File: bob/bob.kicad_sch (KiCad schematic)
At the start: 28 parts, among them J1 PROG, J2 PWR, J3 BB, U1 PAN2110P0AA, U2 LM1117MP-3.3, U3 PY32F030K1xTx, Y1 16MHz

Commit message: WIP
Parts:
- removed C1, C2, C3, C4: NC, Capacitor_SMD:C_0805_2012Metric, symbol Device:C
- removed R2: 0R, Resistor_SMD:R_0805_2012Metric, symbol Device:R
- added JP2: I2C/SPI, Jumper:SolderJumper-3_P2.0mm_Open_TrianglePad1.0x1.5mm, symbol Jumper:SolderJumper_3_Open
- R1: value 0R -> 10k
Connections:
- net +3V3: now also JP2.3 (B)
- net GND: now also JP2.1 (A)
- net PROG_RXD: now also J1.3 (Pin_3); no longer J1.5 (Pin_5)
- net PROG_TXD: now also J1.5 (Pin_5); no longer J1.3 (Pin_3)
- net ~{RF_CS}: now also R1.1
- net at U1.5 (XC1): now also Y1.1
- net at U1.8 (ANT): now also A1.1 (A); no longer R1.1
- net at R1.2: now also JP2.2 (C); no longer A1.1 (A)
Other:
- moved on the sheet: A1, Y1

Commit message: bob 1.3
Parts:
- added R2, R5: 4k7, Resistor_SMD:R_0805_2012Metric, symbol Device:R
- J3: footprint Connector_PinHeader_2.54mm:PinHeader_1x24_P2.54mm_Vertical -> Connector_PinHeader_2.54mm:PinHeader_1x26_P2.54mm_Vertical; symbol Connector:Conn_01x24_Pin -> Connector:Conn_01x26_Pin
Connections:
- net +3V3: now also R2.2, R5.2
- net GND: now also J3.26 (Pin_26); no longer J3.24 (Pin_24)
- net RF_CLK renamed PA9
- net PA9: now also J3.25 (Pin_25), R5.1
- net RF_DIO renamed PA7
- net PA7: now also J3.24 (Pin_24), R2.1

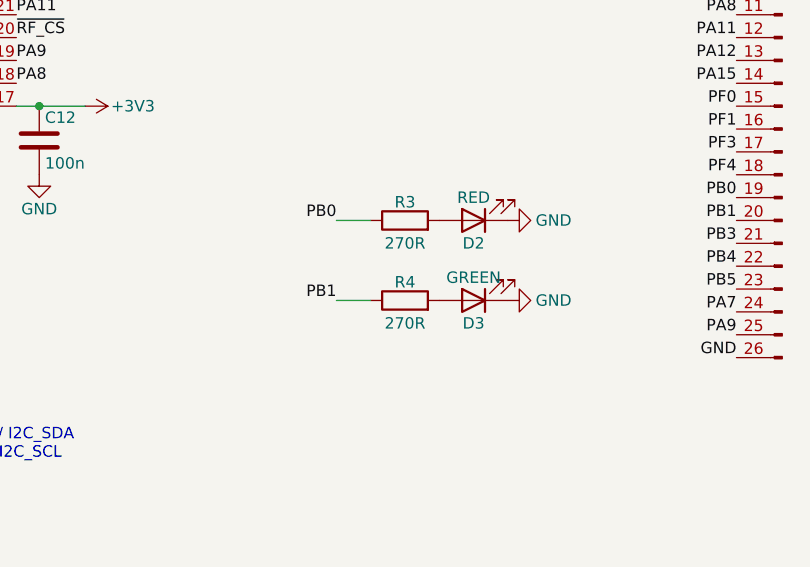
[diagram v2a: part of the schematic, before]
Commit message: LED resistors changed to 330R
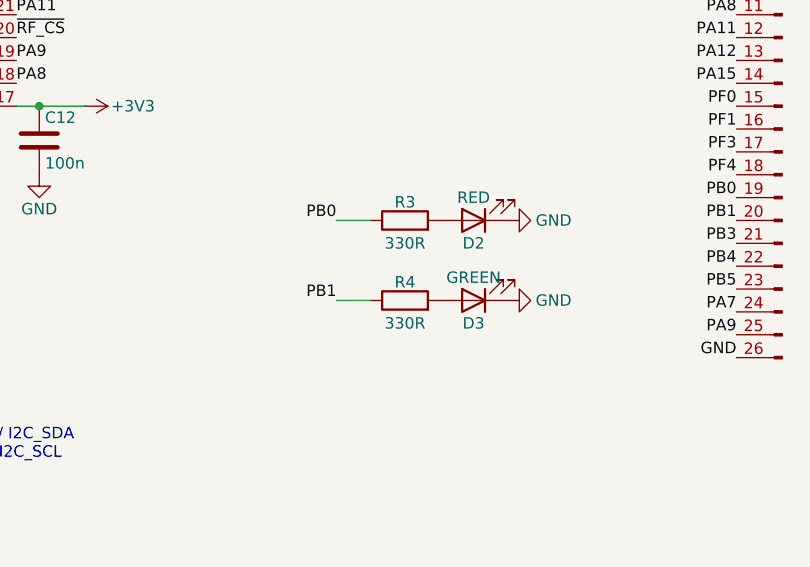
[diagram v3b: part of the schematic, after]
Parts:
- R3, R4: value 270R -> 330R
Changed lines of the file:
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@@
 			)
 		)
-		(property "Value" "270R"
+		(property "Value" "330R"
 			(at 217.17 132.08 90)
 			(effects
@@
 			)
 		)
-		(property "Value" "270R"
+		(property "Value" "330R"
 			(at 217.17 140.97 90)
 			(effects

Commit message: WIP
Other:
- note added: "do verze 1.4 - chyba v pojmenování pinů B4, B5 - již opraveno - jak s SPI/I2C přepínáním - je potřeba?"
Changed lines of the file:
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@@
 		)
 	)
+	(text "do verze 1.4 \n- chyba v pojmenování pinů B4, B5 - již opraveno\n- jak s SPI/I2C přepínáním - je potřeba?"
+		(exclude_from_sim no)
+		(at 186.69 173.482 0)
+		(effects
+			(font
+				(size 1.27 1.27)
+			)
+			(justify left)
+		)
+	)
 	(junction
 		(at 115.57 29.21)
@@
 		)
 		(instances
-			(project ""
+			(project "bob"
 				(path "/3059dabe-d0bb-4700-8034-0af3f3f15902"
 					(reference "U1")
@@
 		)
 		(instances
-			(project ""
+			(project "bob"
 				(path "/3059dabe-d0bb-4700-8034-0af3f3f15902"
 					(reference "D1")
@@
 		)
 		(instances
-			(project ""
+			(project "bob"
 				(path "/3059dabe-d0bb-4700-8034-0af3f3f15902"
 					(reference "A1")
@@
 		)
 		(instances
-			(project ""
+			(project "bob"
 				(path "/3059dabe-d0bb-4700-8034-0af3f3f15902"
 					(reference "J1")
@@
 		)
 		(instances
-			(project ""
+			(project "bob"
 				(path "/3059dabe-d0bb-4700-8034-0af3f3f15902"
 					(reference "JP1")
@@
 		)
 		(instances
-			(project ""
+			(project "bob"
 				(path "/3059dabe-d0bb-4700-8034-0af3f3f15902"
 					(reference "U3")
@@
 		)
 		(instances
-			(project ""
+			(project "bob"
 				(path "/3059dabe-d0bb-4700-8034-0af3f3f15902"
 					(reference "J3")

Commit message: Refactor code structure for improved readability and maintainability
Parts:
- removed JP2: I2C/SPI, Jumper:SolderJumper-3_P2.0mm_Open_TrianglePad1.0x1.5mm, symbol Jumper:SolderJumper_3_Open
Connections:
- net +3V3: now also R1.2
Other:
- note removed: "do verze 1.4 - chyba v pojmenování pinů B4, B5 - již opraveno - jak s SPI/I2C přepínáním - je potřeba?"
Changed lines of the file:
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@@
 		)
 	)
-	(text "do verze 1.4 \n- chyba v pojmenování pinů B4, B5 - již opraveno\n- jak s SPI/I2C přepínáním - je potřeba?"
-		(exclude_from_sim no)
-		(at 186.69 173.482 0)
-		(effects
-			(font
-				(size 1.27 1.27)
-			)
-			(justify left)
-		)
-	)
 	(junction
 		(at 115.57 29.21)
@@
 	)
 	(label "~{RF_CS}"
-		(at 113.03 170.18 0)
+		(at 128.27 170.18 0)
 		(effects
 			(font
@@
 	)
 	(symbol
-		(lib_id "power:GND")
-		(at 148.59 175.26 0)
-		(unit 1)
-		(exclude_from_sim no)
-		(in_bom yes)
-		(on_board yes)
-		(dnp no)
-		(property "Reference" "#PWR01"
-			(at 148.59 181.61 0)
-			(effects
-				(font
-					(size 1.27 1.27)
-				)
-				(hide yes)
-			)
-		)
-		(property "Value" "GND"
-			(at 148.59 179.578 0)
-			(effects
-				(font
-					(size 1.27 1.27)
-				)
-			)
-		)
-		(property "Footprint" ""
-			(at 148.59 175.26 0)
-			(effects
-				(font
-					(size 1.27 1.27)
-				)
-				(hide yes)
-			)
-		)
-		(property "Datasheet" ""
-			(at 148.59 175.26 0)
-			(effects
-				(font
-					(size 1.27 1.27)
-				)
-				(hide yes)
-			)
-		)
-		(property "Description" ""
-			(at 148.59 175.26 0)
-			(effects
-				(font
-					(size 1.27 1.27)
-				)
-			)
-		)
-		(pin "1"
-		)
-		(instances
-			(project "bob"
-				(path "/3059dabe-d0bb-4700-8034-0af3f3f15902"
-					(reference "#PWR01")
-					(unit 1)
-				)
-			)
-		)
-	)
-	(symbol
 		(lib_id "Device:C")
 		(at 115.57 35.56 0)
@@
 	)
 	(symbol
-		(lib_id "Jumper:SolderJumper_3_Open")
-		(at 148.59 170.18 270)
-		(mirror x)
-		(unit 1)
-		(exclude_from_sim no)
-		(in_bom no)
-		(on_board yes)
-		(dnp no)
-		(property "Reference" "JP2"
-			(at 151.13 168.9099 90)
-			(effects
-				(font
-					(size 1.27 1.27)
-				)
-				(justify left)
-			)
-		)
-		(property "Value" "I2C/SPI"
-			(at 151.13 171.4499 90)
-			(effects
-				(font
-					(size 1.27 1.27)
-				)
-				(justify left)
-			)
-		)
-		(property "Footprint" "Jumper:SolderJumper-3_P2.0mm_Open_TrianglePad1.0x1.5mm"
-			(at 148.59 170.18 0)
-			(effects
-				(font
-					(size 1.27 1.27)
-				)
-				(hide yes)
-			)
-		)
-		(property "Datasheet" "~"
-			(at 148.59 170.18 0)
-			(effects
-				(font
-					(size 1.27 1.27)
-				)
-				(hide yes)
-			)
-		)
-		(property "Description" "Solder Jumper, 3-pole, open"
-			(at 148.59 170.18 0)
-			(effects
-				(font
-					(size 1.27 1.27)
-				)
-				(hide yes)
-			)
-		)
-		(pin "2"
-		)
-		(pin "3"
-		)
-		(pin "1"
-		)
-		(instances
-			(project "bob"
-				(path "/3059dabe-d0bb-4700-8034-0af3f3f15902"
-					(reference "JP2")
-					(unit 1)
-				)
-			)
-		)
-	)
-	(symbol
 		(lib_id "Device:C")
 		(at 81.28 152.4 0)
@@
 	(symbol
 		(lib_id "power:+3.3V")
-		(at 148.59 165.1 0)
+		(at 144.78 170.18 270)
 		(unit 1)
 		(exclude_from_sim no)
@@
 		(dnp no)
 		(property "Reference" "#PWR02"
-			(at 148.59 168.91 0)
+			(at 140.97 170.18 0)
 			(effects
 				(font
@@
 		)
 		(property "Value" "+3V3"
-			(at 148.59 161.29 0)
+			(at 148.59 170.18 0)
 			(effects
 				(font
@@
 		)
 		(property "Footprint" ""
-			(at 148.59 165.1 0)
+			(at 144.78 170.18 0)
 			(effects
 				(font
@@
 		)
 		(property "Datasheet" ""
-			(at 148.59 165.1 0)
+			(at 144.78 170.18 0)
 			(effects
 				(font
@@
 		)
 		(property "Description" ""
-			(at 148.59 165.1 0)
+			(at 144.78 170.18 0)
 			(effects
 				(font
